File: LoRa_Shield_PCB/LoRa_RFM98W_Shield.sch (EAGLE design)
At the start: 40 parts, among them IC1 AHT10, IC2 TXS0102DCUR, J1 CON_TERMINAL_BLOCK_03-5MM, J2 TYPE-C-31-M-17, U1 RFM98W, U2 3V3_REG, X2 BU-SMA-H

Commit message: output files updated
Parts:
- removed C10: 22uF, rcl:C-EUC0805
- removed JP9: JUMPER-SMT_2_NC_PASTE_SILK, SparkFun-Jumpers:JUMPER-SMT_2_NC_PASTE_SILK
- added C9: 100nF, rcl:C-EUC0603
- added JP7: (no value), pinhead_v2:PINHD-1X8/OCT
- C2: value 100nF -> 22uF; device rcl:C-EUC0603 -> rcl:C-EUC0805
- C3: value 100uF -> 100nF; device rcl:CPOL-USSMCB -> rcl:C-EUC0603
- C8: value 100nF -> 100uF; device rcl:C-EUC0603 -> rcl:CPOL-USSMCB
- J1: value CON_TERMINAL_BLOCK_03-5MM -> TYPE-C-31-M-17; device dp_devices:CON_TERMINAL_BLOCK_03-5MM -> angrypig7_Library:TYPE-C-31-M-17
- J2: value TYPE-C-31-M-17 -> CON_TERMINAL_BLOCK_03-5MM; device angrypig7_Library:TYPE-C-31-M-17 -> dp_devices:CON_TERMINAL_BLOCK_03-5MM
- JP1: value (none) -> JUMPER-SMT_2_NC_PASTE_SILK; device pinhead_v2:PINHD-1X8/OCT -> SparkFun-Jumpers:JUMPER-SMT_2_NC_PASTE_SILK
- JP2: value (none) -> current measurement; device pinhead_v2:PINHD-1X10/OCT -> pinhead_v2:PINHD-1X2/OCT
- JP3: value (none) -> OLED; device pinhead_v2:PINHD-1X8/OCT -> pinhead_v2:PINHD-1X4/OCT
- JP4: device pinhead_v2:PINHD-1X6/OCT -> pinhead_v2:PINHD-1X8/OCT
- JP5: value OLED -> (none); device pinhead_v2:PINHD-1X4/OCT -> pinhead_v2:PINHD-1X10/OCT
- JP6: value node number -> (none); device pinhead_v2:PINHD-1X3/OCT -> pinhead_v2:PINHD-1X6/OCT
- JP8: value current measurement -> node number; device pinhead_v2:PINHD-1X2/OCT -> pinhead_v2:PINHD-1X3/OCT
- R10, R12, R8: value 5k -> 10k
- R11, R9: value 10k -> 5k
- R2: value 10k -> 165k
- R4: value 10k -> 15k
- R6: value 165k -> 10k
- R7: value 15k -> 5k
- U1: value RFM98W -> 3V3_REG; device SparkFun-RF:RFM95W -> SamacSys_Parts:AZ1117H-5.0TRE1
- U2: value 3V3_REG -> RFM98W; device SamacSys_Parts:AZ1117H-5.0TRE1 -> SparkFun-RF:RFM95W
- renumbered B2 to B1, D4 to D2, X2 to X1
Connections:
- net 3.3V: now also C2.2, C5.2, C7.1, C8.+, C9.1, R5.2, R6.2, U1.OUT, U1.VOUT, U2.3.3V; no longer C10.2, C2.1, C3.+, C4.2, C5.1, R2.2, R3.2, U1.3.3V, U2.OUT, U2.VOUT
- net 5V: now also JP1.2, JP2.1, JP3.1, JP4.4, U1.IN; no longer JP3.4, JP5.1, JP8.1, JP9.2, U2.IN
- net GND: now also C2.1, C3.2, C5.1, C8.-, C9.2, J1.GND, J1.GND_2, J1.SHIELD, J2.2, JP4.2, JP4.3, JP5.4, JP8.1, JP8.2, R10.2, R12.2, R3.1, R4.1, R8.2; no longer C10.1, C2.2, C3.-, C5.2, C8.1, J1.2, J2.GND, J2.GND_2, J2.SHIELD, JP2.4, JP3.3, JP5.2, JP6.1, JP6.2, R11.2, R4.2, R5.1, R7.1, R9.2
- net I2C_SCL_3V3: now also R6.1; no longer R2.1
- net I2C_SCL_5V: now also JP3.3, JP6.1; no longer JP4.1, JP5.3
- net I2C_SDA_3V3: now also R5.1; no longer R3.1
- net I2C_SDA_5V: now also JP3.4, JP6.2; no longer JP4.2, JP5.4
- net INPUT_RELAY_STATUS: now also C4.2, J2.1, JP6.5, R3.2; no longer C8.2, J1.1, JP4.5, R5.2
- net INPUT_VOLTAGE_READING: now also C3.1, JP6.6, R2.1, R4.2; no longer C7.1, JP4.6, R6.1, R7.2
- net N$1: now also J1.VBUS, J1.VBUS_2; no longer J2.VBUS, J2.VBUS_2
- net N$10: now also JP7.4; no longer JP1.4
- net N$12: now also JP5.9; no longer JP2.9
- net N$13: now also JP5.10; no longer JP2.10
- net N$14: now also JP7.1; no longer JP1.1
- net N$15: now also JP7.2; no longer JP1.2
- net N$16: now also JP1.1, JP2.2; no longer JP8.2, JP9.1
- net N$2: now also U2.ANT; no longer U1.ANT
- net N$20: now also JP7.7; no longer JP1.7
- net N$21: now also JP7.8; no longer JP1.8
- net N$23: now also JP4.5; no longer JP3.5
- net N$24: now also JP4.6; no longer JP3.6
- net N$25: now also JP4.7; no longer JP3.7
- net N$26: now also JP4.8; no longer JP3.8
- net N$29: now also JP6.4; no longer JP4.4
- net N$3: now also JP5.1; no longer JP2.1
- net N$30: now also JP8.3; no longer JP4.3
- net N$5: now also JP5.2; no longer JP2.2
- net N$6: now also JP5.3; no longer JP2.3
- net N$7: now also JP4.1; no longer JP3.1
- net N$8: now also J2.3, R2.2; no longer J1.3, R6.2
- net RFM_DIO0: now also JP7.6, U2.DIO0; no longer JP1.6, U1.DIO0
- net RFM_DIO1: now also JP7.5, U2.DIO1; no longer JP1.5, U1.DIO1
- net RFM_RESET: now also JP7.3, U2.!RESET; no longer JP1.3, U1.!RESET
- net SPI_CLK_3V3: now also R11.2, R12.1, U2.SCK; no longer R4.1, R8.2, U1.SCK
- net SPI_CLK_5V: now also JP5.5, R11.1; no longer JP2.5, R8.1
- net SPI_MISO: now also JP5.6, U2.MISO; no longer JP2.6, U1.MISO
- net SPI_MOSI_3V3: now also R10.1, R9.2, U2.MOSI; no longer R10.2, R9.1, U1.MOSI
- net SPI_MOSI_5V: now also JP5.7, R9.1; no longer JP2.7, R10.1
- net SPI_SS_RFM_3V3: now also R7.2, R8.1, U2.NSS; no longer R11.1, R12.2, U1.NSS
- net SPI_SS_RFM_5V: now also JP5.8, R7.1; no longer JP2.8, R12.1

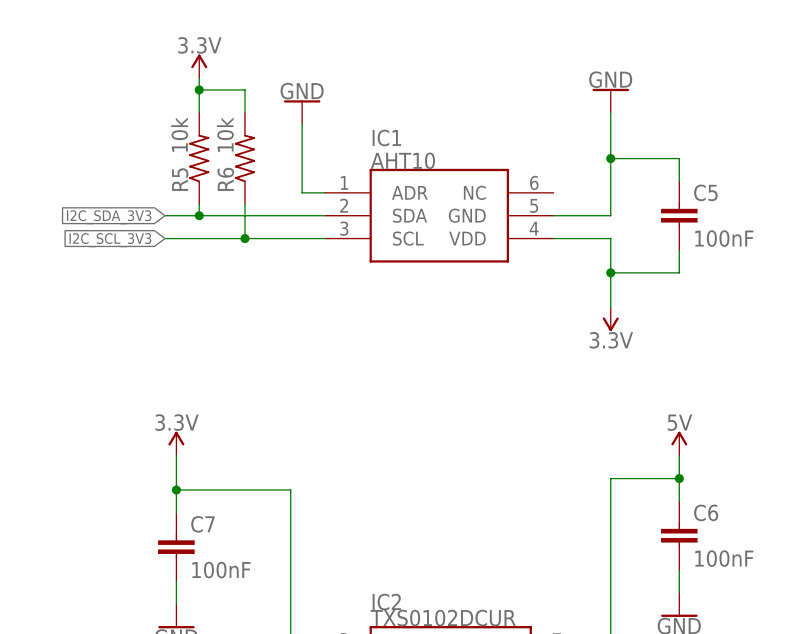
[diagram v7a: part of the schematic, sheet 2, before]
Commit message: parts updated for LCSC orders
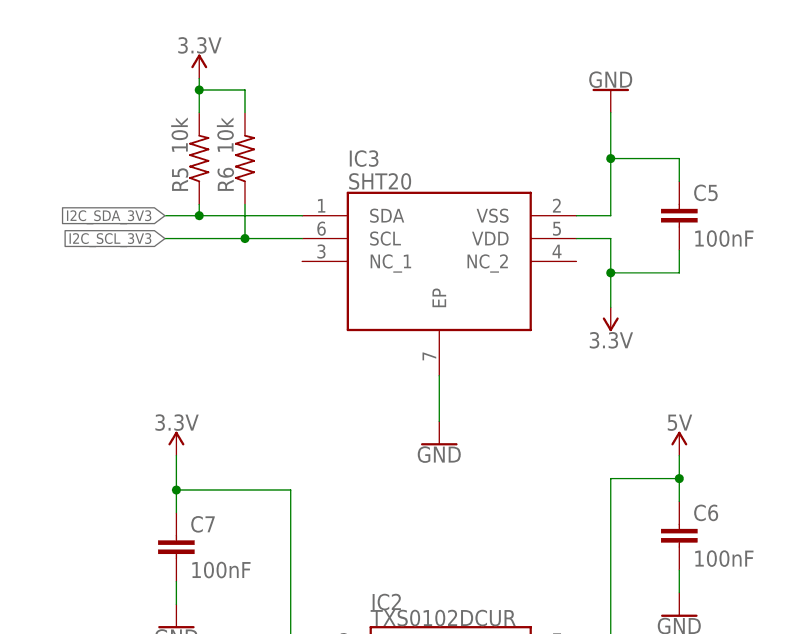
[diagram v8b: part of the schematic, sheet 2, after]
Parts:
- removed IC1: AHT10, SamacSys_Parts:AHT10
- added IC3: SHT20, SamacSys_Parts:SHT20
- LED1: value green -> (none); device adafruit:LEDCHIP-LED0603 -> led:LEDCHIPLED_0805
- U1: value 3V3_REG -> XC6206P332MR; device SamacSys_Parts:AZ1117H-5.0TRE1 -> SamacSys_Parts:XC6206P332MR
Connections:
- net 3.3V: now also IC3.VDD; no longer IC1.VDD, U1.OUT
- net 5V: now also U1.VIN; no longer U1.IN
- net GND: now also IC3.EP, IC3.VSS, U1.VSS; no longer IC1.ADR, IC1.GND, U1.GND
- net I2C_SCL_3V3: now also IC3.SCL; no longer IC1.SCL
- net I2C_SDA_3V3: now also IC3.SDA; no longer IC1.SDA
